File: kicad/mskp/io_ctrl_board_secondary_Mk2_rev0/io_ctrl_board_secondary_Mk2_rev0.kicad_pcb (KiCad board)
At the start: 2 copper layers, 25 parts, among them J1 USB_C_I2C_input, J2 Keypad_matrix_connector_JST, J3 OLED_128x64, J4 I2C_aux_JST, J5 RJ45_SPI_I2C_input, J6 SPI_aux_JST, J7 I2C_aux_pads, U1 MCP23017_SP, U2 AMS1117-3v3

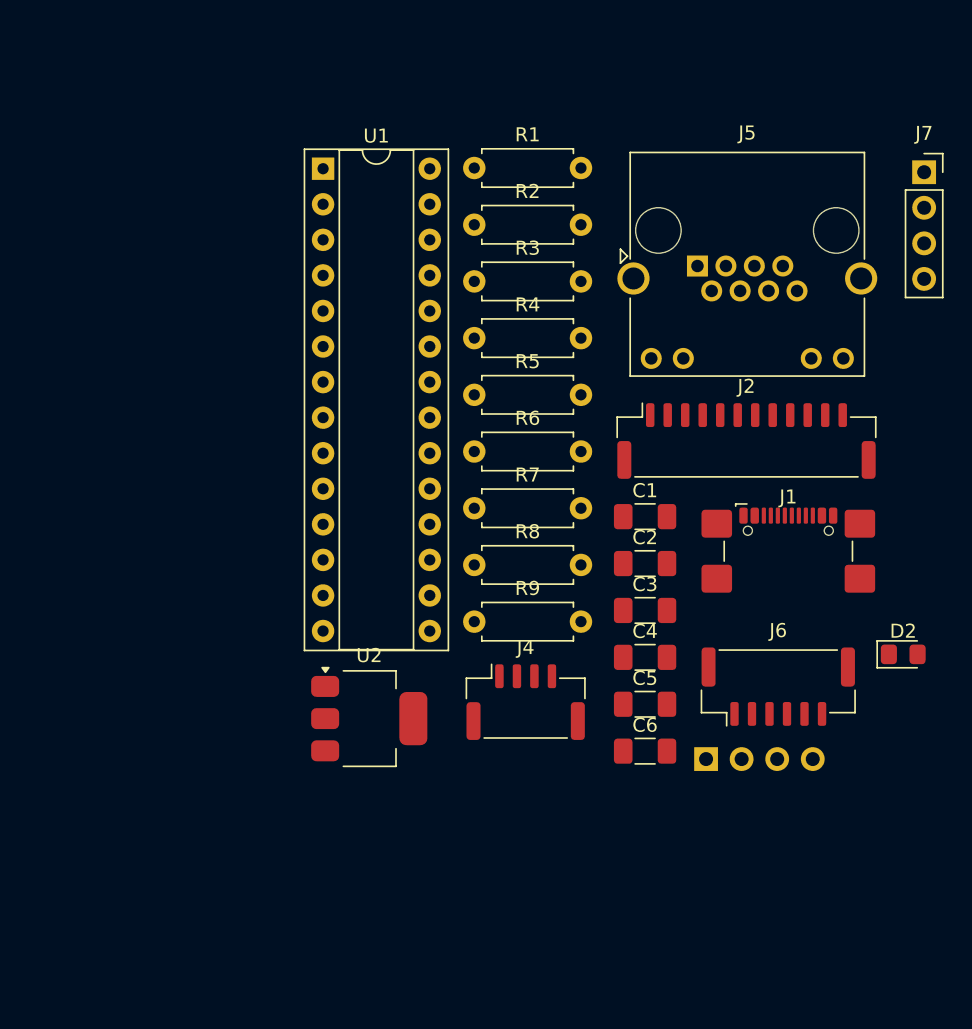
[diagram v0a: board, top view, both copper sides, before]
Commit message: Begins rough PCB part grouping for all control board revisions
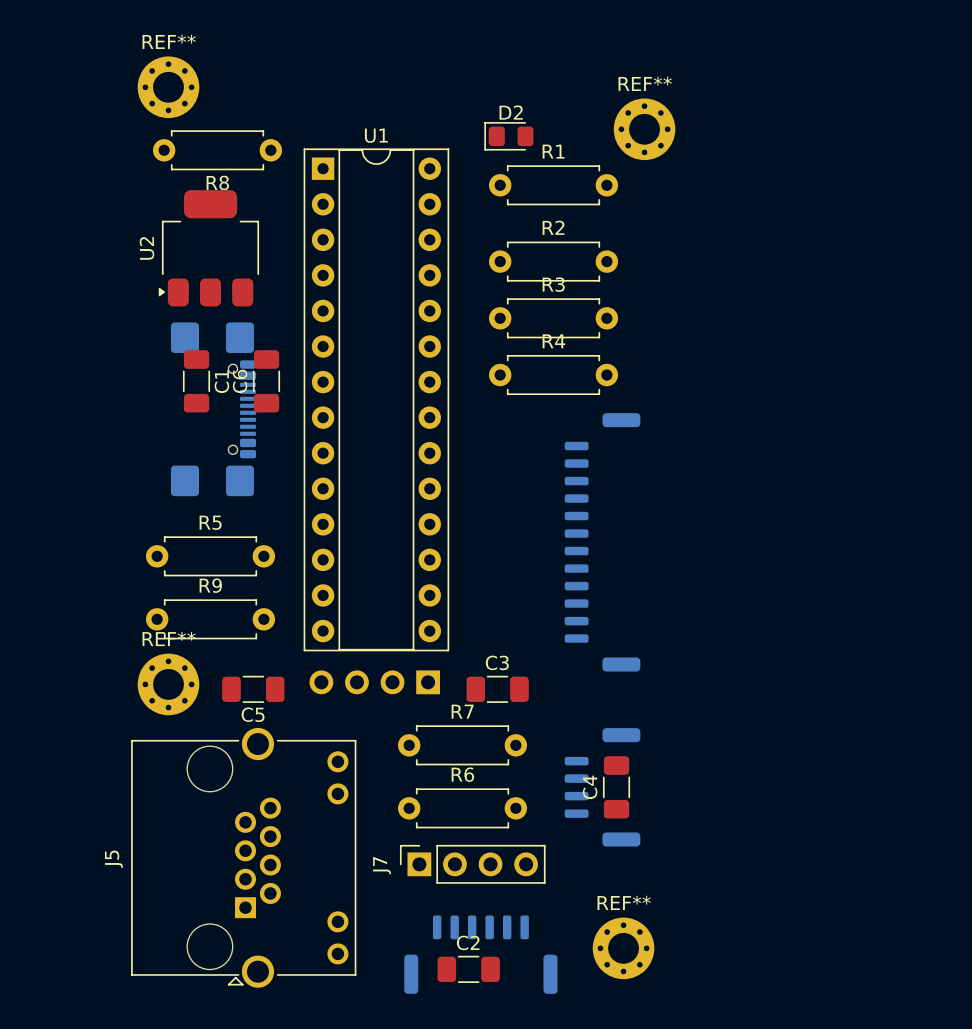
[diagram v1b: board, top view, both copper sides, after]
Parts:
- added REF**: MountingHole_2.2mm_M2_Pad_Via, MountingHole:MountingHole_2.2mm_M2_Pad_Via, F.Cu at (149.5, 60.5)
- added REF**: MountingHole_2.2mm_M2_Pad_Via, MountingHole:MountingHole_2.2mm_M2_Pad_Via, F.Cu at (115.5, 100.2)
- added REF**: MountingHole_2.2mm_M2_Pad_Via, MountingHole:MountingHole_2.2mm_M2_Pad_Via, F.Cu at (115.5, 57.5)
- added REF**: MountingHole_2.2mm_M2_Pad_Via, MountingHole:MountingHole_2.2mm_M2_Pad_Via, F.Cu at (148.0, 119.0)
- J1, J2, J4, J6: moved to B.Cu
- moved J7 61.2 mm to (133.4, 113.0), turned to 90 degrees
- moved J5 56.1 mm to (121.0, 116.1), turned to 90 degrees
- moved D2 46.4 mm to (140.0, 61.0)
- moved J1 43.7 mm to (117.5, 80.5), turned to 90 degrees
- moved C6 37.8 mm to (122.5, 78.5), turned to 90 degrees
- moved U2 35.5 mm to (118.5, 69.0), turned to 90 degrees
- moved C1 33.5 mm to (117.5, 78.5), turned to -90 degrees
- moved R8 33.0 mm to (122.8, 62.0), turned to 180 degrees
- moved C2 31.6 mm to (136.9, 120.5)
- moved J6 28.6 mm to (137.8, 119.5)
- moved J3 28.0 mm to (130.2, 100.0), turned to 180 degrees
- moved C5 28.0 mm to (121.6, 100.5), turned to 180 degrees
- moved R6 25.9 mm to (132.7, 109.0)
- moved R5 25.4 mm to (114.7, 91.0)
- moved R9 22.7 mm to (114.7, 95.5)
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
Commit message: Continues work with rough PCB outlines
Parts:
- moved C1 17.9 mm to (123.0, 61.5)
- moved R5 14.8 mm to (114.7, 76.2)
- moved R9 14.8 mm to (114.7, 80.8)
- moved J1 9.12 mm to (117.9, 89.6)
- moved C6 8.84 mm to (116.2, 84.8), turned to 0 degrees
- moved R8 4.41 mm to (126.4, 59.5), turned to 0 degrees
- moved REF** 3.82 mm to (117.5, 60.8)
- moved REF** 3.58 mm to (145.9, 60.5)
- moved J2 1.57 mm to (147.1, 91.5)
- moved R1 1.50 mm to (139.2, 66.0)
- moved J5 1.25 mm to (119.8, 116.1)
- moved REF** 1.12 mm to (147.0, 118.5)
- moved REF** 0.75 mm to (116.2, 100.2)
- moved J4 0.70 mm to (147.2, 107.5)
- moved C5 0.38 mm to (121.9, 100.5)
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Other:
- board outline added: 37.2 x 65.8 mm

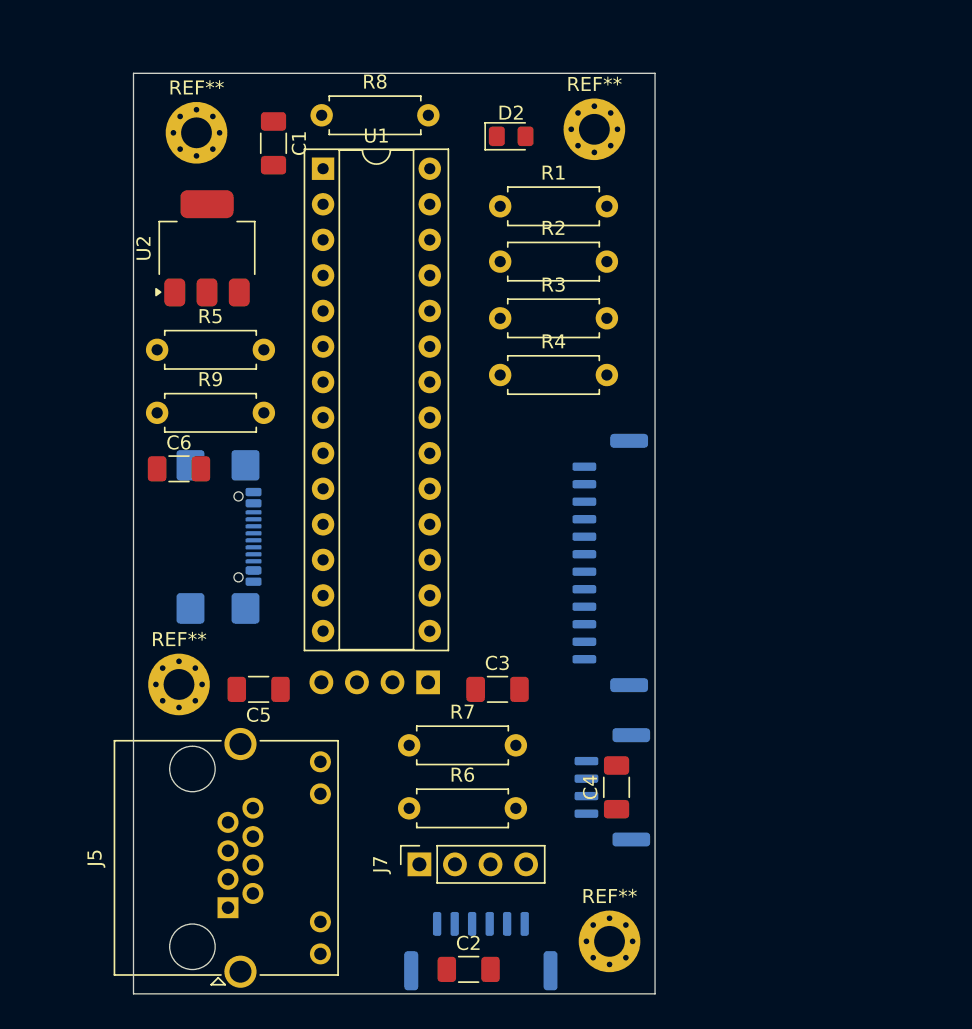
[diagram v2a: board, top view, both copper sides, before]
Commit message: Refining PCB outlines for pico and io control boards
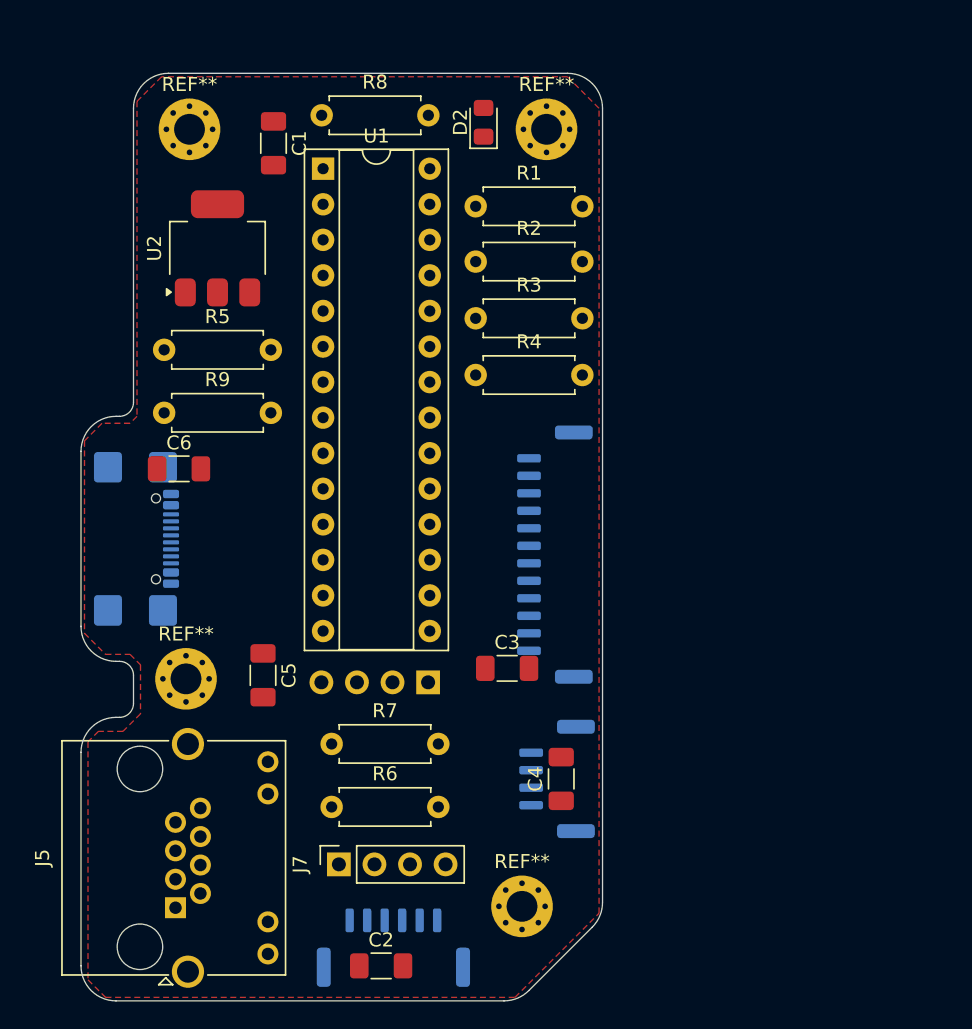
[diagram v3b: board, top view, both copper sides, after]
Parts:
- moved REF** 6.73 mm to (140.8, 116.0)
- moved C2 6.25 mm to (130.7, 120.2)
- moved J6 6.25 mm to (131.6, 119.0)
- moved J1 5.90 mm to (112.0, 89.8)
- moved J7 5.75 mm to (127.7, 113.0)
- moved R6 5.54 mm to (127.2, 108.9)
- moved R7 5.54 mm to (127.2, 104.4)
- moved J2 4.00 mm to (143.1, 90.9)
- moved C4 4.00 mm to (143.6, 106.9)
- moved J4 4.00 mm to (143.2, 106.9)
- moved J5 3.75 mm to (116.0, 116.1)
- moved REF** 3.42 mm to (142.5, 60.5)
- moved D2 2.21 mm to (138.0, 60.0), turned to 90 degrees
- moved R1 1.75 mm to (137.4, 66.0)
- moved R2 1.75 mm to (137.4, 70.0)
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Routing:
- added copper zone on F.Cu, net GND
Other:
- board size 37.2 x 65.8 mm -> 37.2 x 66.2 mm

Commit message: Initial layout of PCB traces on io_ctrl_board_secondary_Mk2_rev0
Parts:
- J6: footprint Connector_JST:JST_GH_BM06B-GHS-TBT_1x06-1MP_P1.25mm_Vertical -> Connector_JST:JST_GH_SM06B-GHS-TB_1x06-1MP_P1.25mm_Horizontal
- moved R1 18.7 mm to (136.9, 84.7)
- moved R2 18.7 mm to (136.9, 88.6)
- moved R3 18.7 mm to (136.9, 92.7)
- moved R4 18.7 mm to (136.9, 96.7)
- moved J2 17.7 mm to (143.0, 73.2)
- moved C3 1.59 mm to (139.0, 100.4)
- moved C2 0.85 mm to (131.5, 120.2)
- moved J6 0.75 mm to (131.5, 119.7), turned to 180 degrees
- moved J3 0.58 mm to (129.7, 100.0)
- moved U1 0.29 mm to (126.2, 63.3)
- moved C5 0.25 mm to (122.0, 99.5)
- turned C1 to 90 degrees
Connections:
- C3 pad 1: +5V -> /3V3
- J3 pad 2: +5V -> /3V3
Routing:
- net +5V: track 0.00 -> 99.3 mm, vias 0 -> 6
- net /3V3: track 0.00 -> 95.5 mm, vias 0 -> 2
- net /SCL: track 0.00 -> 75.0 mm, vias 0 -> 6
- net /SDA: track 0.00 -> 65.6 mm, vias 0 -> 2
- net Net-(U1-GPB0): track 0.00 -> 52.6 mm, vias 0 -> 2
- net GND: track 0.00 -> 45.8 mm, vias 0 -> 3
- net Net-(U1-GPB1): track 0.00 -> 45.6 mm, vias 0 -> 1
- net Net-(J2-Pin_4): track 0.00 -> 35.2 mm
- net Net-(J2-Pin_3): track 0.00 -> 32.2 mm
- net Net-(J2-Pin_2): track 0.00 -> 29.3 mm
- net /CSn: track 0.00 -> 28.4 mm
- net Net-(J2-Pin_1): track 0.00 -> 26.8 mm
- net Net-(J2-Pin_12): track 0.00 -> 26.4 mm, vias 0 -> 1
- net Net-(J2-Pin_11): track 0.00 -> 23.2 mm, vias 0 -> 1
- net /TX: track 0.00 -> 22.0 mm
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
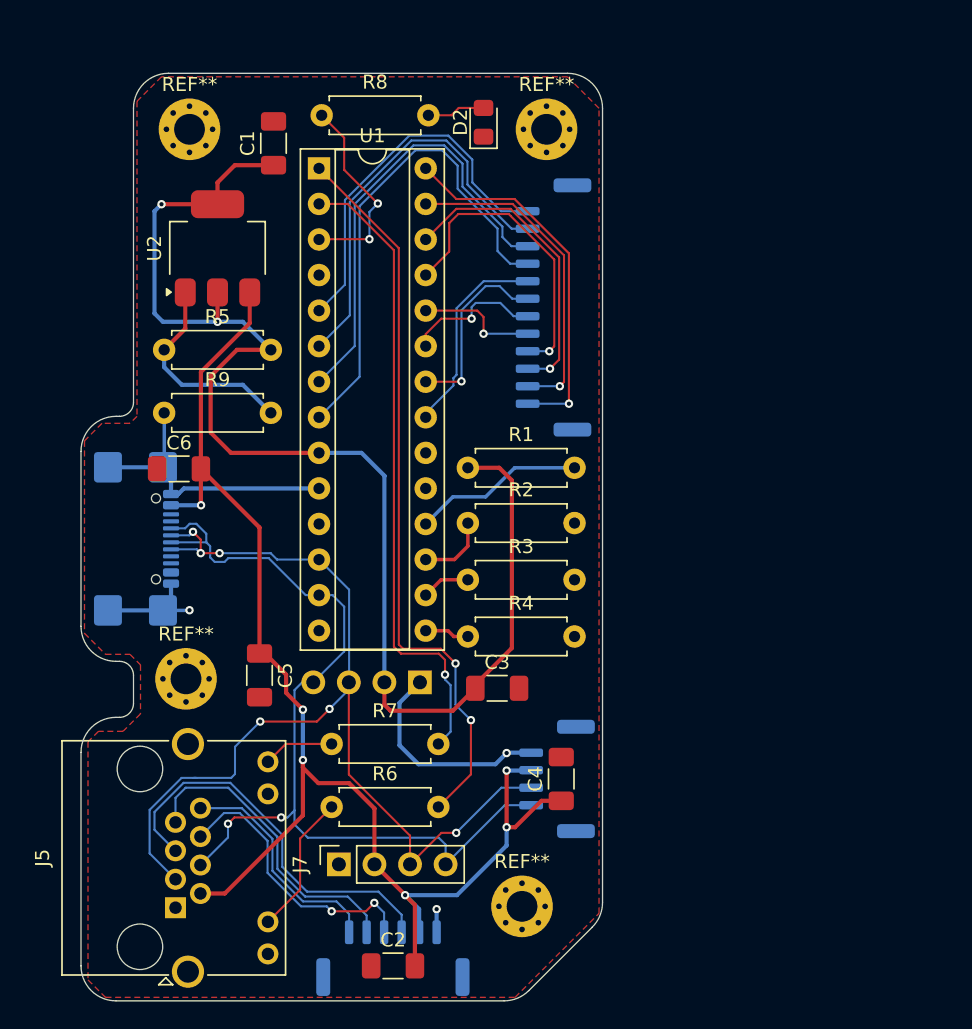
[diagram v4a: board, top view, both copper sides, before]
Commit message: Adds io_ctrl_board_secondary_Mk2_rev0 silkscreen
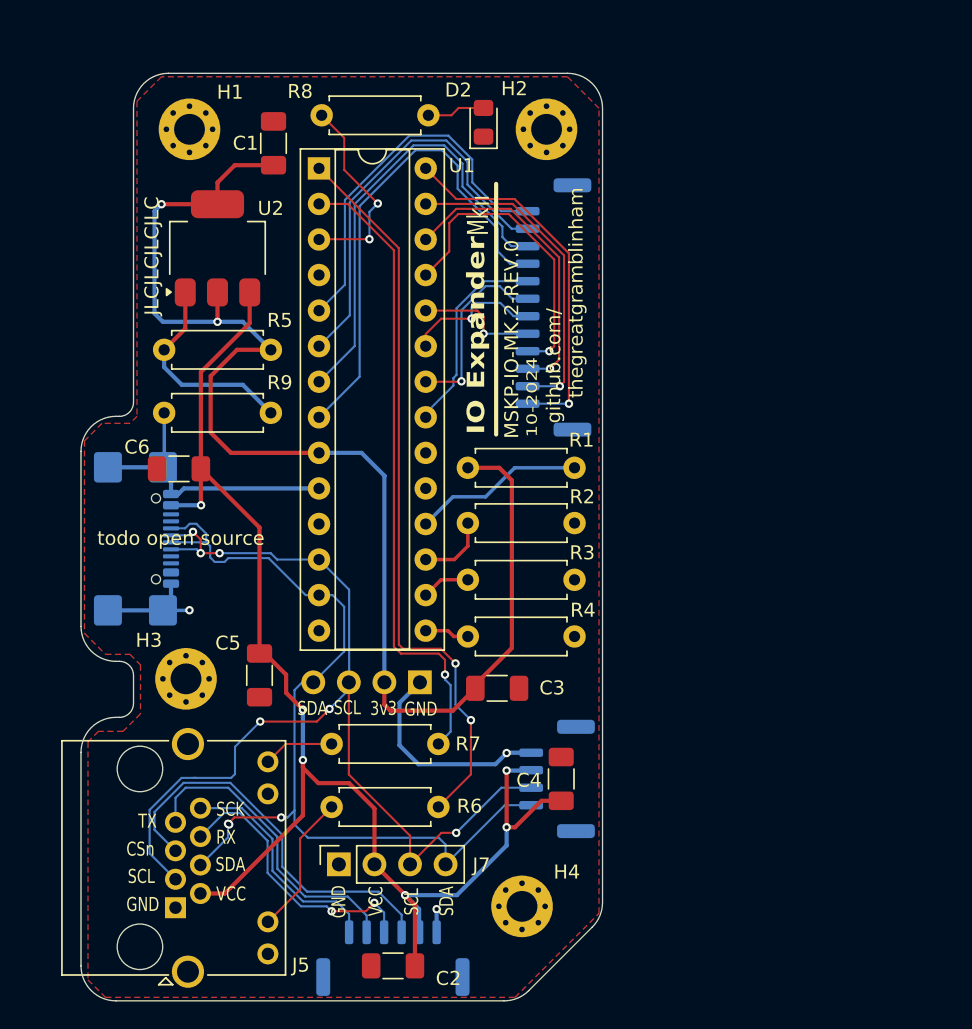
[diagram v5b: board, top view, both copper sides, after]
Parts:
- renumbered REF** to H1, REF** to H2, REF** to H3, REF** to H4
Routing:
- net /SDA: vias 2 -> 3
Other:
- board text added: "10-2024"
- board text added: "3v3"
- board text added: "CSn"
- board text added: "GND"
- board text added: "I2C"
- board text added: "I2C + SPI"
- board text added: "II"
- board text added: "IO Expander"
- board text added: "JLCJLCJLCJLC"
- board text added: "KEYPAD MODULE"
- board text added: "MSKP-IO-MK.2-REV.0"
- board text added: "Mk"
- board text added: "RX"
- board text added: "SCK"
- board text added: "SCL"
- board text added: "SDA"
- board text added: "SPI"
- board text added: "TX"
- board text added: "VCC"
- board text added: "github.com/"
- board text added: "thegreatgramblinham"
- board text added: "todo open source"

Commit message: Final tweaks to PCBs before second round of mskp fabrications
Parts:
- moved J6 0.25 mm to (131.5, 119.5)
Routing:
- net +5V: track 99.3 -> 109.0 mm, vias 6 -> 7
- net /SDA: vias 3 -> 2
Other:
- board text removed: "todo open source"
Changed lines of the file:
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@@
 			(plot_on_all_layers_selection 0x0000000_00000000)
 			(disableapertmacros no)
-			(usegerberextensions no)
-			(usegerberattributes yes)
-			(usegerberadvancedattributes yes)
-			(creategerberjobfile yes)
+			(usegerberextensions yes)
+			(usegerberattributes no)
+			(usegerberadvancedattributes no)
+			(creategerberjobfile no)
 			(dashed_line_dash_ratio 12.000000)
 			(dashed_line_gap_ratio 3.000000)
 			(svgprecision 4)
 			(plotframeref no)
-			(viasonmask no)
+			(viasonmask yes)
 			(mode 1)
 			(useauxorigin no)
@@
 			(psa4output no)
 			(plotreference yes)
-			(plotvalue yes)
+			(plotvalue no)
 			(plotfptext yes)
 			(plotinvisibletext no)
 			(sketchpadsonfab no)
-			(subtractmaskfromsilk no)
+			(subtractmaskfromsilk yes)
 			(outputformat 1)
 			(mirror no)
-			(drillshape 1)
+			(drillshape 0)
 			(scaleselection 1)
-			(outputdirectory "")
+			(outputdirectory "io_ctrl_mk2_exports")
 		)
 	)
@@
 	(footprint "Connector_JST:JST_GH_SM06B-GHS-TB_1x06-1MP_P1.25mm_Horizontal"
 		(layer "B.Cu")
-		(at 131.525 119.7 180)
+		(at 131.525 119.45 180)
 		(descr "JST GH series connector, SM06B-GHS-TB (http://www.jst-mfg.com/product/pdf/eng/eGH.pdf), generated with kicad-footprint-generator")
 		(tags "connector JST GH horizontal")
@@
 	)
 	(gr_text "SPI"
-		(at 133.5 116.2 0)
+		(at 133.5 116.1 0)
 		(layer "B.SilkS")
 		(effects
@@
 	)
 	(gr_text "JLCJLCJLCJLC"
-		(at 114.9 73.8 90)
+		(at 110.5 87.9 0)
 		(layer "F.SilkS")
 		(effects
@@
 		)
 	)
-	(gr_text "todo open source"
-		(at 110.4 90.3 0)
-		(layer "F.SilkS")
-		(effects
-			(font
-				(size 1 1)
-				(thickness 0.1)
-			)
-			(justify left bottom)
-		)
-	)
 	(gr_text "SDA"
-		(at 135.95 116.7 90)
+		(at 135.95 116.6 90)
 		(layer "F.SilkS")
 		(effects
@@
 	)
 	(gr_text "GND"
-		(at 128.25 116.85 90)
+		(at 128.25 116.75 90)
 		(layer "F.SilkS")
 		(effects
@@
 	)
 	(gr_text "VCC"
-		(at 130.9 116.7 90)
+		(at 130.9 116.6 90)
 		(layer "F.SilkS")
 		(effects
@@
 				(size 1 1)
 				(thickness 0.1)
+				(italic yes)
 			)
 			(justify left bottom)
@@
 	)
 	(gr_text "SCL"
-		(at 133.45 116.65 90)
+		(at 133.45 116.55 90)
 		(layer "F.SilkS")
 		(effects
@@
 				(size 1 1)
 				(thickness 0.1)
+				(italic yes)
 			)
 			(justify left bottom)
@@
 	)
 	(segment
+		(start 122 97.9375)
+		(end 122 96.3)
+		(width 0.3)
+		(layer "F.Cu")
+		(net 3)
+	)
+	(segment
 		(start 125.1 105.55)
 		(end 125.1 109.5)
@@
 	)
 	(segment
+		(start 122 96.3)
+		(end 117.8 92.1)
+		(width 0.3)
+		(layer "F.Cu")
+		(net 3)
+	)
+	(segment
 		(start 140.25 110.35)
 		(end 142.1375 108.4625)
@@
 	)
 	(via blind
+		(at 117.8 92.1)
+		(size 0.6)
+		(drill 0.3)
+		(layers "F.Cu" "B.Cu")
+		(net 3)
+	)
+	(via blind
 		(at 117.825 87.35)
 		(size 0.6)
@@
 	)
 	(segment
+		(start 115.73 92.1)
+		(end 115.68 92.15)
+		(width 0.3)
+		(layer "B.Cu")
+		(net 3)
+	)
+	(segment
 		(start 136.1 115.2)
 		(end 139.65 111.65)
@@
 	)
 	(segment
+		(start 117.8 92.1)
+		(end 115.73 92.1)
+		(width 0.3)
+		(layer "B.Cu")
+		(net 3)
+	)
+	(segment
 		(start 133.4 116.2)
 		(end 133.4 117.85)
@@
 	)
 	(segment
-		(start 117.475 106.825)
-		(end 117.3 106.825)
-		(width 0.15)
-		(layer "B.Cu")
-		(net 5)
-	)
-	(segment
 		(start 119.15 90.775)
 		(end 122.8 90.775)
@@
 	)
 	(via blind
-		(at 119.835714 110.15)
+		(at 119.75 110.1)
 		(size 0.6)
 		(drill 0.3)
@@
 		(size 0.6)
 		(drill 0.3)
-		(layers "F.Cu" "B.Cu")
-		(net 6)
-	)
-	(via blind
-		(at 119.75 110.1)
-		(size 0.6)
-		(drill 0.3)
